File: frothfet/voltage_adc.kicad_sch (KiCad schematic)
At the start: 4 parts, among them U23 ADS1015IDGS

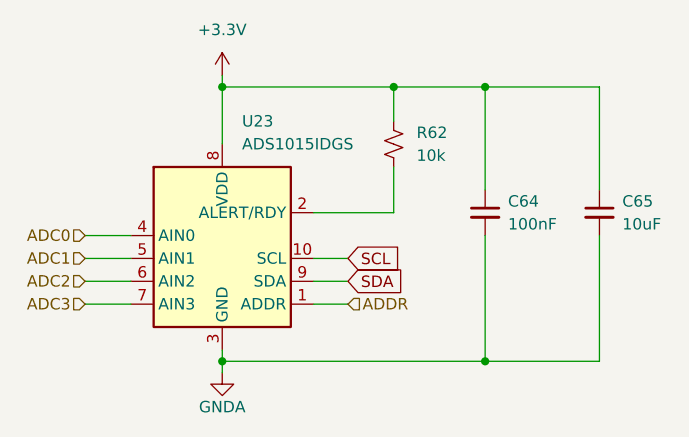
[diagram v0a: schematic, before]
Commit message: Revert "prep for new HierarchialPCB test"
This reverts commit 7ba467f7ba771a9ed3b62c58bdcef6315b0965ad.
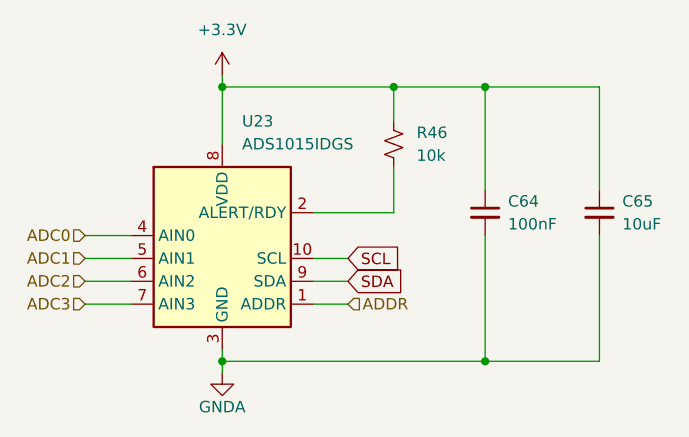
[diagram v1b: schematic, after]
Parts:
- renumbered R62 to R46
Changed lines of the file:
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@@
 		(dnp no)
 		(fields_autoplaced yes)
-		(property "Reference" "R62"
+		(property "Reference" "R46"
 			(at 160.02 82.55 0)
 			(effects
@@
 			(project "8ch-mosfet"
 				(path "/c83c6236-96e9-46ad-9d7a-9e2efa4a7966/a6260305-24e3-4714-b441-a7a157c17bd9"
-					(reference "R62")
+					(reference "R46")
 					(unit 1)
 				)
 				(path "/c83c6236-96e9-46ad-9d7a-9e2efa4a7966/bb9dea8b-8412-49bc-950d-dce57727bcd2"
-					(reference "R61")
+					(reference "R45")
 					(unit 1)
 				)
@@
 		(on_board yes)
 		(dnp no)
-		(property "Reference" "#PWR080"
+		(property "Reference" "#PWR072"
 			(at 138.43 115.57 0)
 			(effects
@@
 			(project "8ch-mosfet"
 				(path "/c83c6236-96e9-46ad-9d7a-9e2efa4a7966/a6260305-24e3-4714-b441-a7a157c17bd9"
-					(reference "#PWR080")
+					(reference "#PWR072")
 					(unit 1)
 				)
 				(path "/c83c6236-96e9-46ad-9d7a-9e2efa4a7966/bb9dea8b-8412-49bc-950d-dce57727bcd2"
-					(reference "#PWR078")
+					(reference "#PWR070")
 					(unit 1)
 				)
@@
 		(dnp no)
 		(fields_autoplaced yes)
-		(property "Reference" "#PWR079"
+		(property "Reference" "#PWR071"
 			(at 138.43 80.01 0)
 			(effects
@@
 			(project "8ch-mosfet"
 				(path "/c83c6236-96e9-46ad-9d7a-9e2efa4a7966/a6260305-24e3-4714-b441-a7a157c17bd9"
-					(reference "#PWR079")
+					(reference "#PWR071")
 					(unit 1)
 				)
 				(path "/c83c6236-96e9-46ad-9d7a-9e2efa4a7966/bb9dea8b-8412-49bc-950d-dce57727bcd2"
-					(reference "#PWR077")
-					(unit 1)
-				)
+					(reference "#PWR069")
+					(unit 1)
+				)

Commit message: prep for new HierarchialPCB test
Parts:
- renumbered R46 to R62
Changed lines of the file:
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@@
 		(dnp no)
 		(fields_autoplaced yes)
-		(property "Reference" "R46"
+		(property "Reference" "R62"
 			(at 160.02 82.55 0)
 			(effects
@@
 			(project "8ch-mosfet"
 				(path "/c83c6236-96e9-46ad-9d7a-9e2efa4a7966/a6260305-24e3-4714-b441-a7a157c17bd9"
-					(reference "R46")
+					(reference "R62")
 					(unit 1)
 				)
 				(path "/c83c6236-96e9-46ad-9d7a-9e2efa4a7966/bb9dea8b-8412-49bc-950d-dce57727bcd2"
-					(reference "R45")
+					(reference "R61")
 					(unit 1)
 				)
@@
 		(on_board yes)
 		(dnp no)
-		(property "Reference" "#PWR072"
+		(property "Reference" "#PWR080"
 			(at 138.43 115.57 0)
 			(effects
@@
 			(project "8ch-mosfet"
 				(path "/c83c6236-96e9-46ad-9d7a-9e2efa4a7966/a6260305-24e3-4714-b441-a7a157c17bd9"
-					(reference "#PWR072")
+					(reference "#PWR080")
 					(unit 1)
 				)
 				(path "/c83c6236-96e9-46ad-9d7a-9e2efa4a7966/bb9dea8b-8412-49bc-950d-dce57727bcd2"
-					(reference "#PWR070")
+					(reference "#PWR078")
 					(unit 1)
 				)
@@
 		(dnp no)
 		(fields_autoplaced yes)
-		(property "Reference" "#PWR071"
+		(property "Reference" "#PWR079"
 			(at 138.43 80.01 0)
 			(effects
@@
 			(project "8ch-mosfet"
 				(path "/c83c6236-96e9-46ad-9d7a-9e2efa4a7966/a6260305-24e3-4714-b441-a7a157c17bd9"
-					(reference "#PWR071")
+					(reference "#PWR079")
 					(unit 1)
 				)
 				(path "/c83c6236-96e9-46ad-9d7a-9e2efa4a7966/bb9dea8b-8412-49bc-950d-dce57727bcd2"
-					(reference "#PWR069")
-					(unit 1)
-				)
+					(reference "#PWR077")
+					(unit 1)
+				)
